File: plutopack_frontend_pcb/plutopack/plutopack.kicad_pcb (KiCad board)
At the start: 4 copper layers, 77 x 129 mm, 143 parts, among them J1 Conn_02x10_Odd_Even, J2 Conn_01x50, J3 Battery_Cell, J4 Conn_01x06_Pin, J5 USB_C_Receptacle_PowerOnly_6P, J6 Conn_02x05_Odd_Even, Q1 AO3401A, Q2 AO3400A, Q3 AO3400A, Q4 AO3401A, SW1 SW_Push, SW10 SW_SPDT, SW2 RotaryEncoder, SW3 SW_Push, SW4 SW_Push, SW5 SW_Push, SW6 SW_Push, SW7 SW_Push, SW8 SW_Push, U1 BQ24075RGT, U2 TSC2007IPWR, U3 TPS63020, U4 BQ27441-G1, U5 TPS63020, U6 BQ297xy, U7 TXS0108EPW

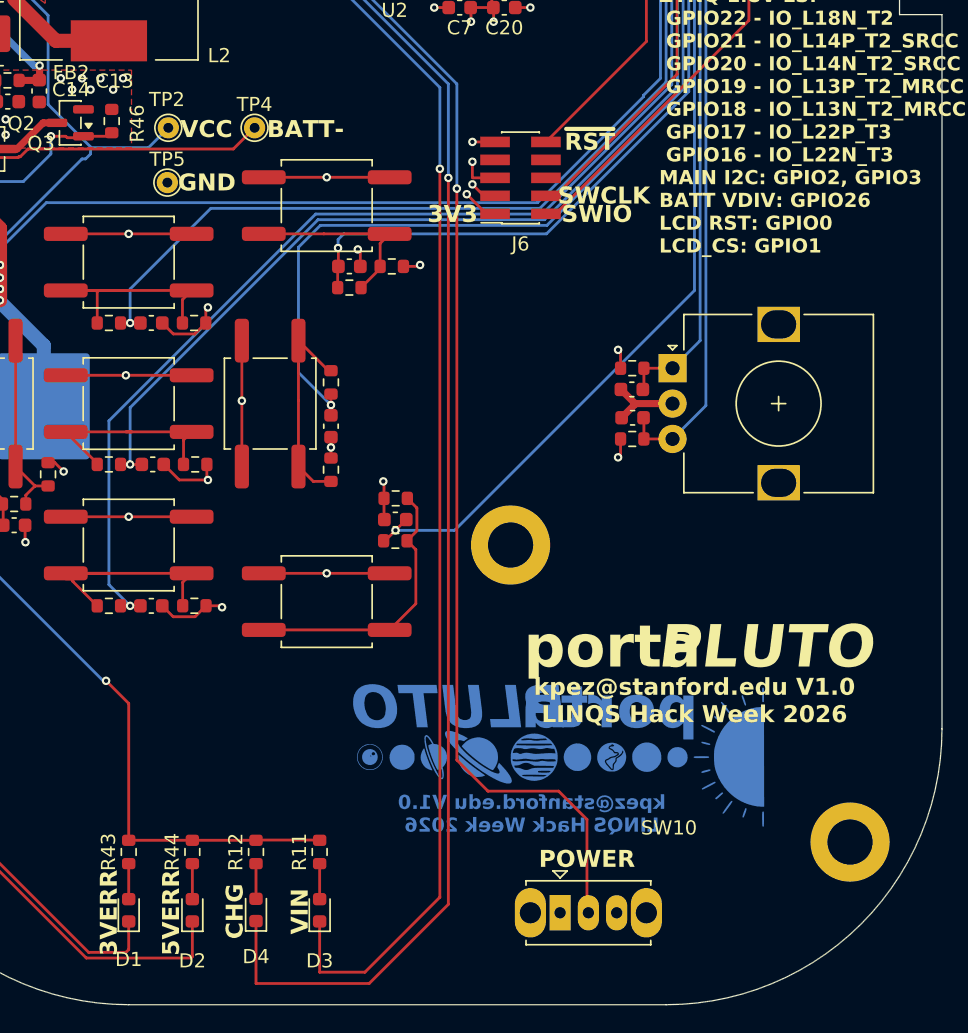
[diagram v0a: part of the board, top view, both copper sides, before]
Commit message: Update frontend PCB to latest revision
Sync plutopack_frontend_pcb with the latest KiCad layout, power_management
schematic changes, and regenerated JLC production outputs (BOM, positions,
netlist, gerber zip).

Co-Authored-By: Claude Opus 5.5 (1M context) <noreply@anthropic.com>
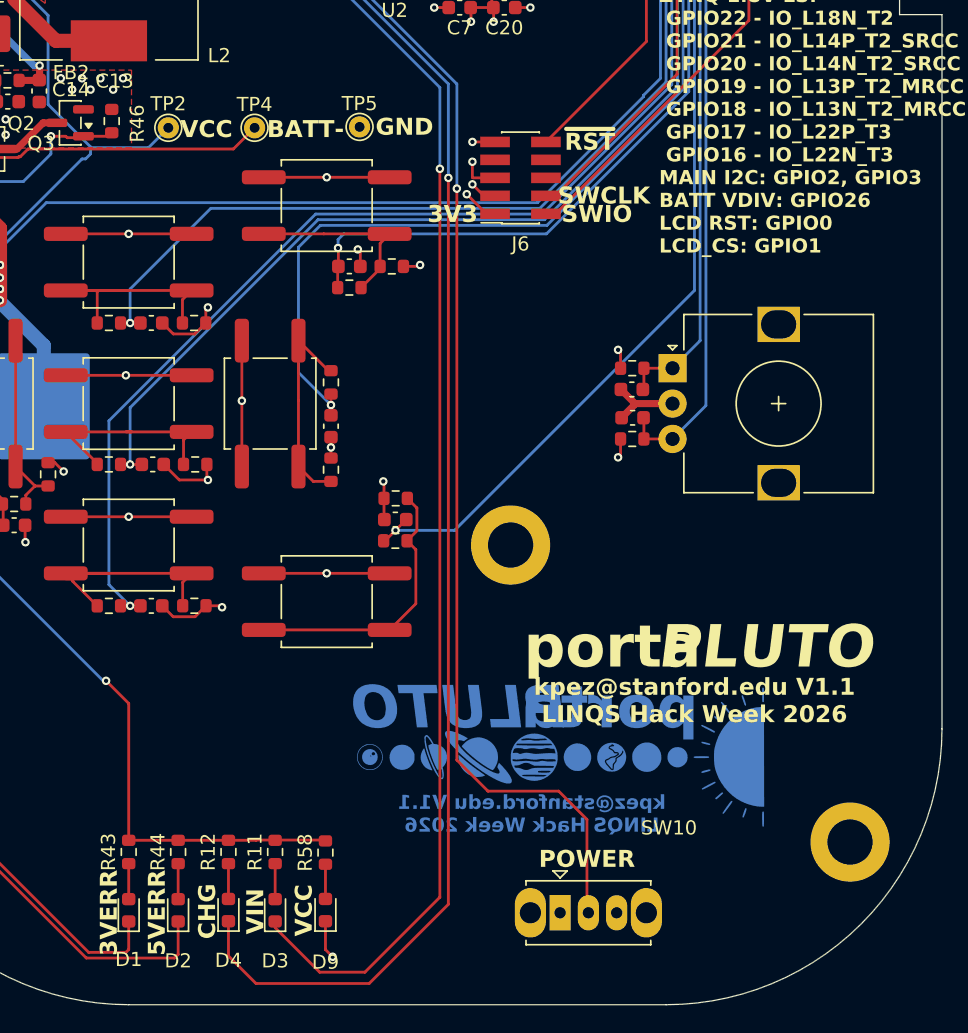
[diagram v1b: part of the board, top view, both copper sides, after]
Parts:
- added D9: LED, LED_SMD:LED_0603_1608Metric, F.Cu at (33.9, 122.8)
- added R58: 1k, Resistor_SMD:R_0603_1608Metric, F.Cu at (33.9, 118.7)
- moved TP5 14.1 mm to (36.3, 67.4)
- moved D3 3.15 mm to (30.4, 122.8)
- moved R11 3.15 mm to (30.4, 118.7)
- moved D4 1.95 mm to (27.1, 122.8)
- moved R12 1.95 mm to (27.1, 118.7)
- moved D2 1.00 mm to (23.5, 122.8)
- moved R44 1.00 mm to (23.5, 118.7)
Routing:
- net GND: track 109.9 -> 112.6 mm, vias 120 -> 121
- net Net-(D9-A): track 0.00 -> 2.45 mm
- net Net-(D3-K): track 128.7 -> 129.9 mm
- net /power_management/5V_PG: track 115.9 -> 114.8 mm
- net Net-(D4-K): track 133.3 -> 134.1 mm
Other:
- board text added: "kpez@stanford.edu V1.1 LINQS Hack Week 2026"
- board text removed: "kpez@stanford.edu V1.0 LINQS Hack Week 2026"
